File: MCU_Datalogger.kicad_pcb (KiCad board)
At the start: 2 copper layers, 53 x 32.6 mm, 29 parts, among them J1 Conn_01x04_Pin, J2 Conn_01x04_Pin, J3 Conn_01x09_Pin, J4 Conn_02x03_Odd_Even, U1 24LC1025, U2 24LC1025, U3 DS1337S_, U4 ATMEGA328P-AU, Y1 32.768 KHz, Y2 16 MHz

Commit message: Fixed various errors and made the PCB more redeable
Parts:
- renumbered C2 to C, J1 to J8
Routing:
- net GND: track 0.00 -> 59.0 mm, vias 0 -> 17
- net /RESET: track 26.6 -> 26.7 mm, vias 5 -> 4
- added copper zone on B.Cu, net GND
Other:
- board text added: "D2"
- board text added: "D3"
- board text added: "D4"
- board text added: "D5"
- board text added: "D6"
- board text added: "D7"
- board text added: "D8"
- board text added: "GND"
- board text added: "MISO"
- board text added: "MOSI"
- board text added: "RST"
- board text added: "SCK"
- board text added: "SDA"
- board text added: "Vcc"

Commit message: Added silkscreens and labels
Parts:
- added REF**: KiCad-Logo2_5mm_SilkScreen, Symbol:KiCad-Logo2_5mm_SilkScreen, B.Cu at (109.5, 128.2)
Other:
- board text added: "Data logger w/ ATMega328P"
- board text added: "Made by Larsson Cruze"
- board text added: "RX"
- board text added: "TX"
- board text added: "V.1 2 Layers"

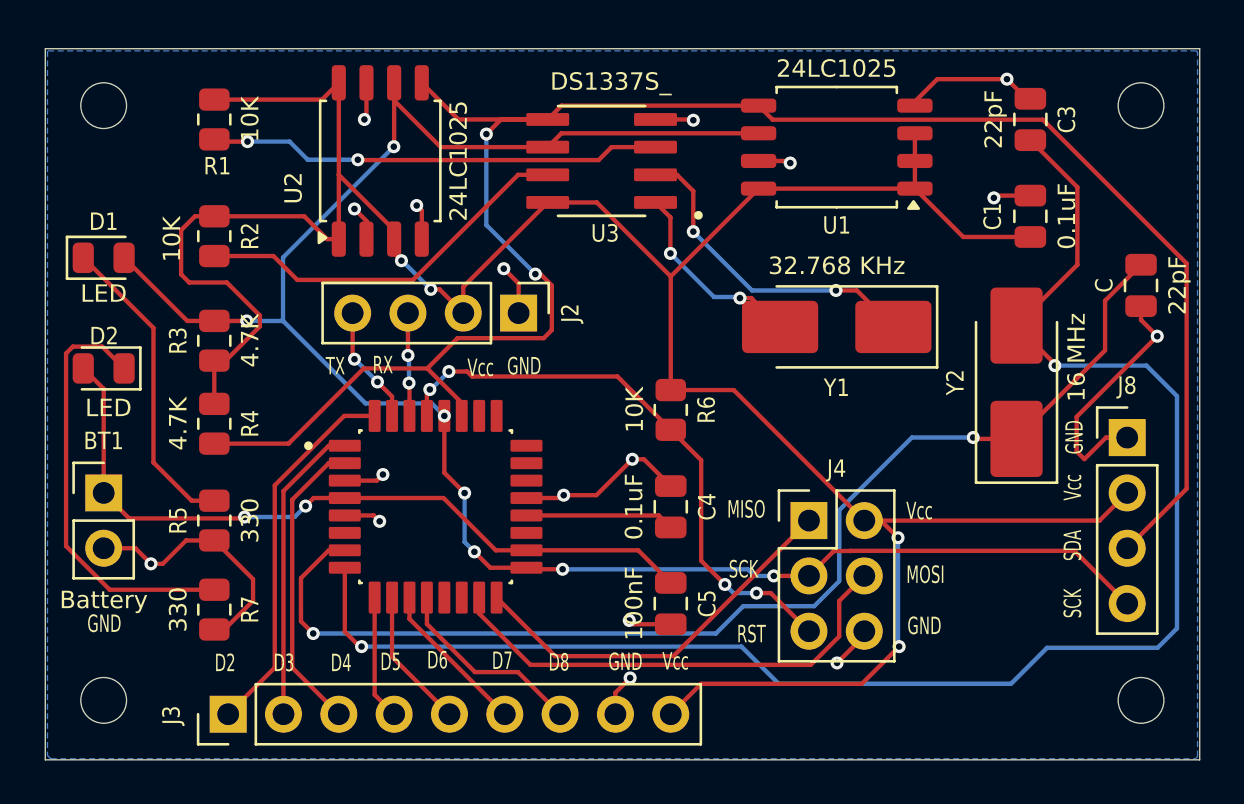
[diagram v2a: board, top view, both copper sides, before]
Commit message: Additional bug fixes with rerouting of Routes
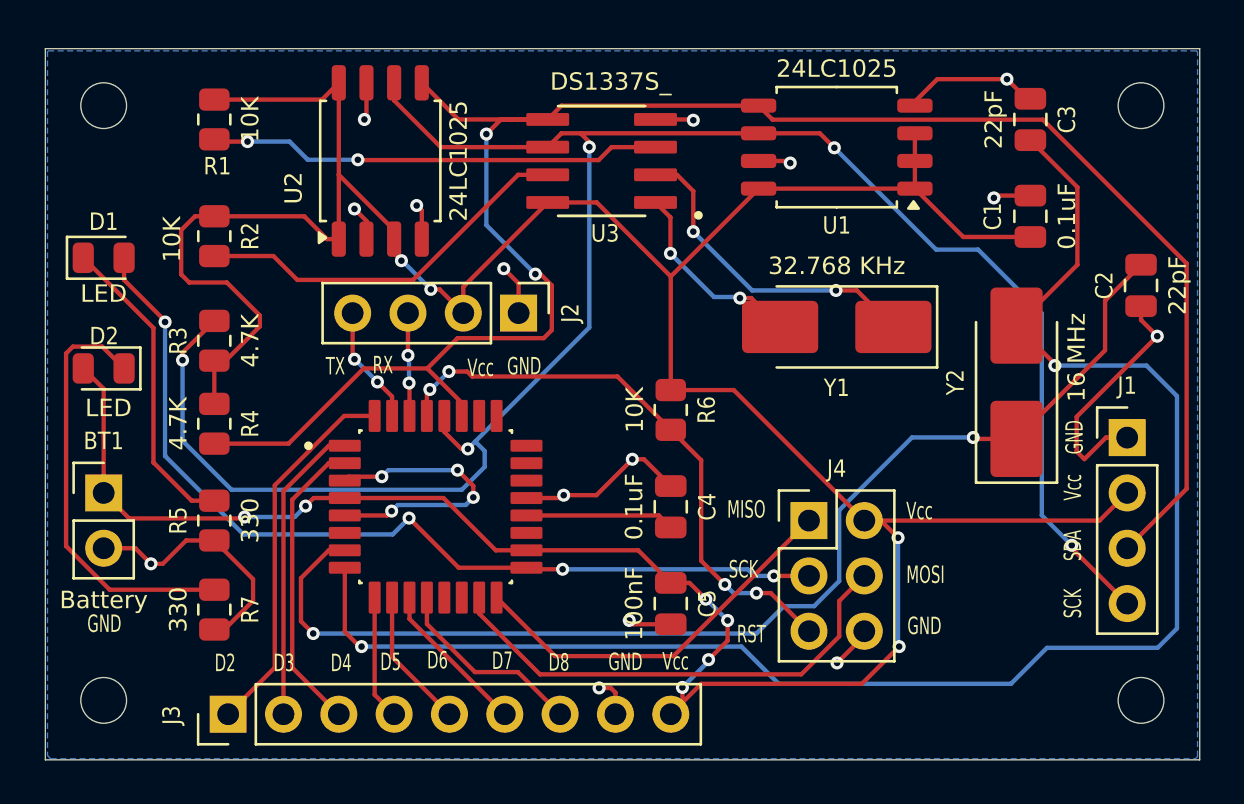
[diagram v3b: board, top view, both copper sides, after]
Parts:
- renumbered C to C2, J8 to J1
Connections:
- BT1 pad 1: Net-(BT1-+) -> /Vcc
- C5 pad 1: Net-(BT1-+) -> /Vcc
- D2 pad 2: Net-(BT1-+) -> /Vcc
- J1 pad 4: /SCK -> /SCL
- R3 pad 2: /SCK -> /SCL
- U1 pad 6: /SCK -> /SCL
- U2 pad 6: /SCK -> /SCL
- U3 pad 6: /SCK -> /SCL
- U4 pad 18: Net-(BT1-+) -> /Vcc
- U4 pad 28: /SCK -> /SCL
- U4 pad 4: Net-(BT1-+) -> /Vcc
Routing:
- net /SCL: track 0.00 -> 91.9 mm, vias 0 -> 5
- net /SCK: track 88.2 -> 42.3 mm, vias 7 -> 4
- net /Vcc: track 124.4 -> 167.7 mm, vias 4 -> 10
- net Net-(BT1-+): track 34.6 -> 0.00 mm, vias 2 -> 0
- net GND: track 59.0 -> 68.5 mm, vias 17 -> 19
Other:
- board text added: "2 Layers PCB"
- board text added: "Version 1"
- board text removed: "V.1 2 Layers"

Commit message: Check point of Project Completion
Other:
- board text added: "0.0000 mm / 0.0000 mm"
- board text added: "0.3000 mm"
- board text added: "1.6000 mm"
- board text added: "2"
- board text added: "53.0000 mm x 32.6500 mm"
- board text added: "BOARD CHARACTERISTICS"
- board text added: "Board Thickness:"
- board text added: "Board overall dimensions:"
- board text added: "Castellated pads:"
- board text added: "Copper Finish:"
- board text added: "Copper Layer Count:"
- board text added: "Edge card connectors:"
- board text added: "Impedance Control:"
- board text added: "Min hole diameter:"
- board text added: "Min track/spacing:"
- board text added: "No"
- board text added: "None"
- board text added: "Plated Board Edge:"
